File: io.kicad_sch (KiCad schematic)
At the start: 14 parts, among them SW6 TS-1088-AR02016, SW7 TS-1088-AR02016, SW8 TS-1088-AR02016, SW9 TS-1088-AR02016

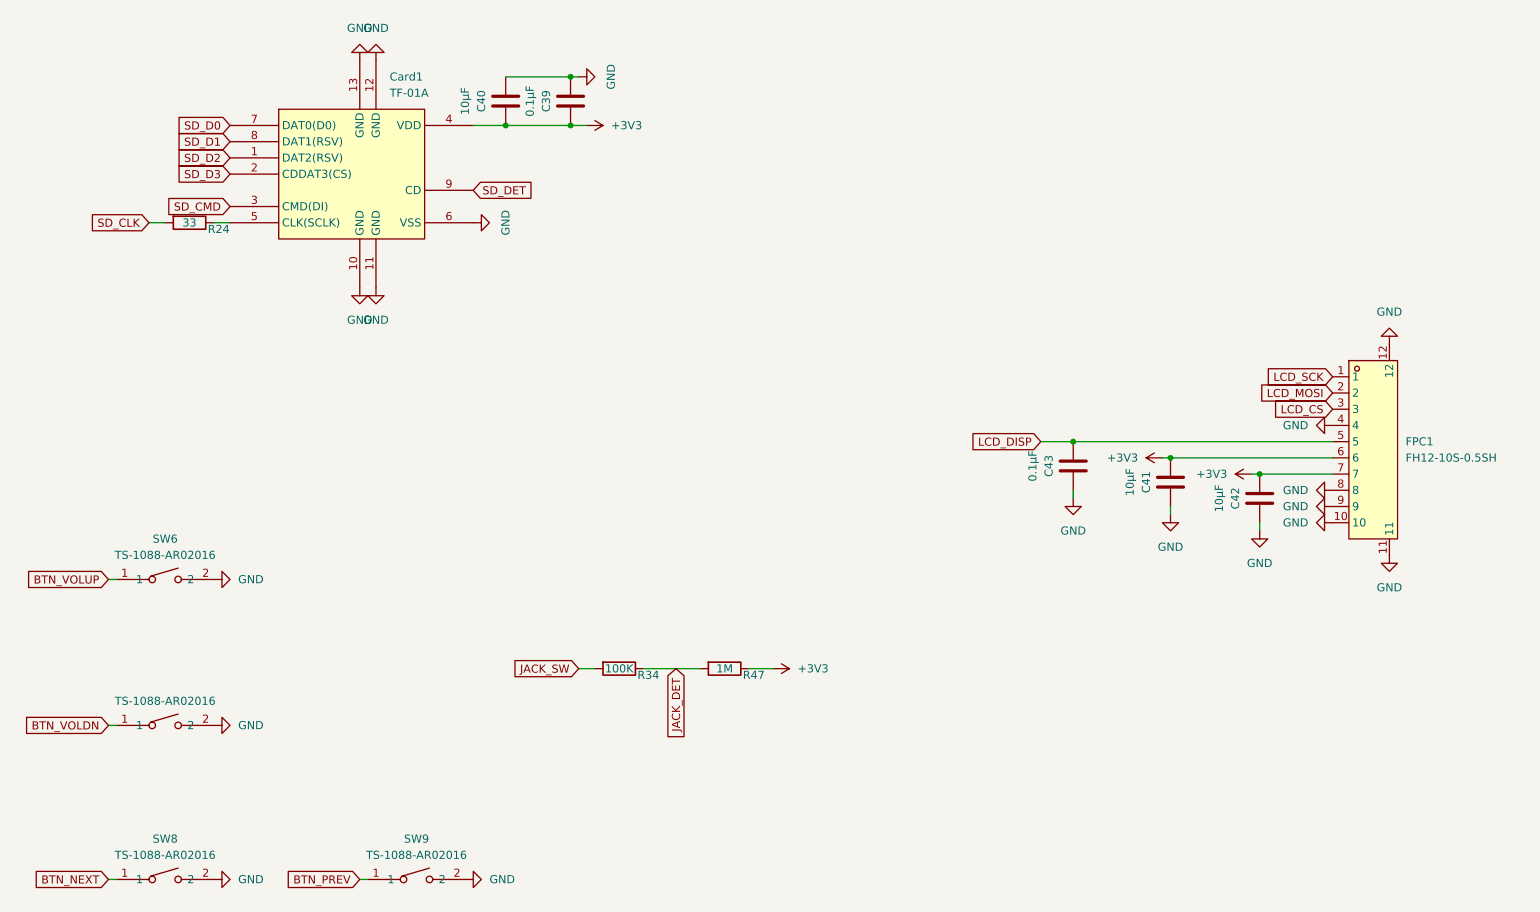
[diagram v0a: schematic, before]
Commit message: Schematic done
- sheet files renamed to English (usb, power, esp32, audio, io)
- final layout, annotation R1-R42 / C1-C43 / U1-U9 / J1-J4 / SW1-SW8
- all buttons are TS-1088, project R/C symbols, PWR_FLAGs
- connections.md replaces conexiuni.md (English, final references)
- final check on the KiCad netlist: 278/278 checks against connections.md
- status updated; firmware note: BQ25180 charge current defaults to ~10 mA

Co-Authored-By: Claude Opus 5.5 <noreply@anthropic.com>
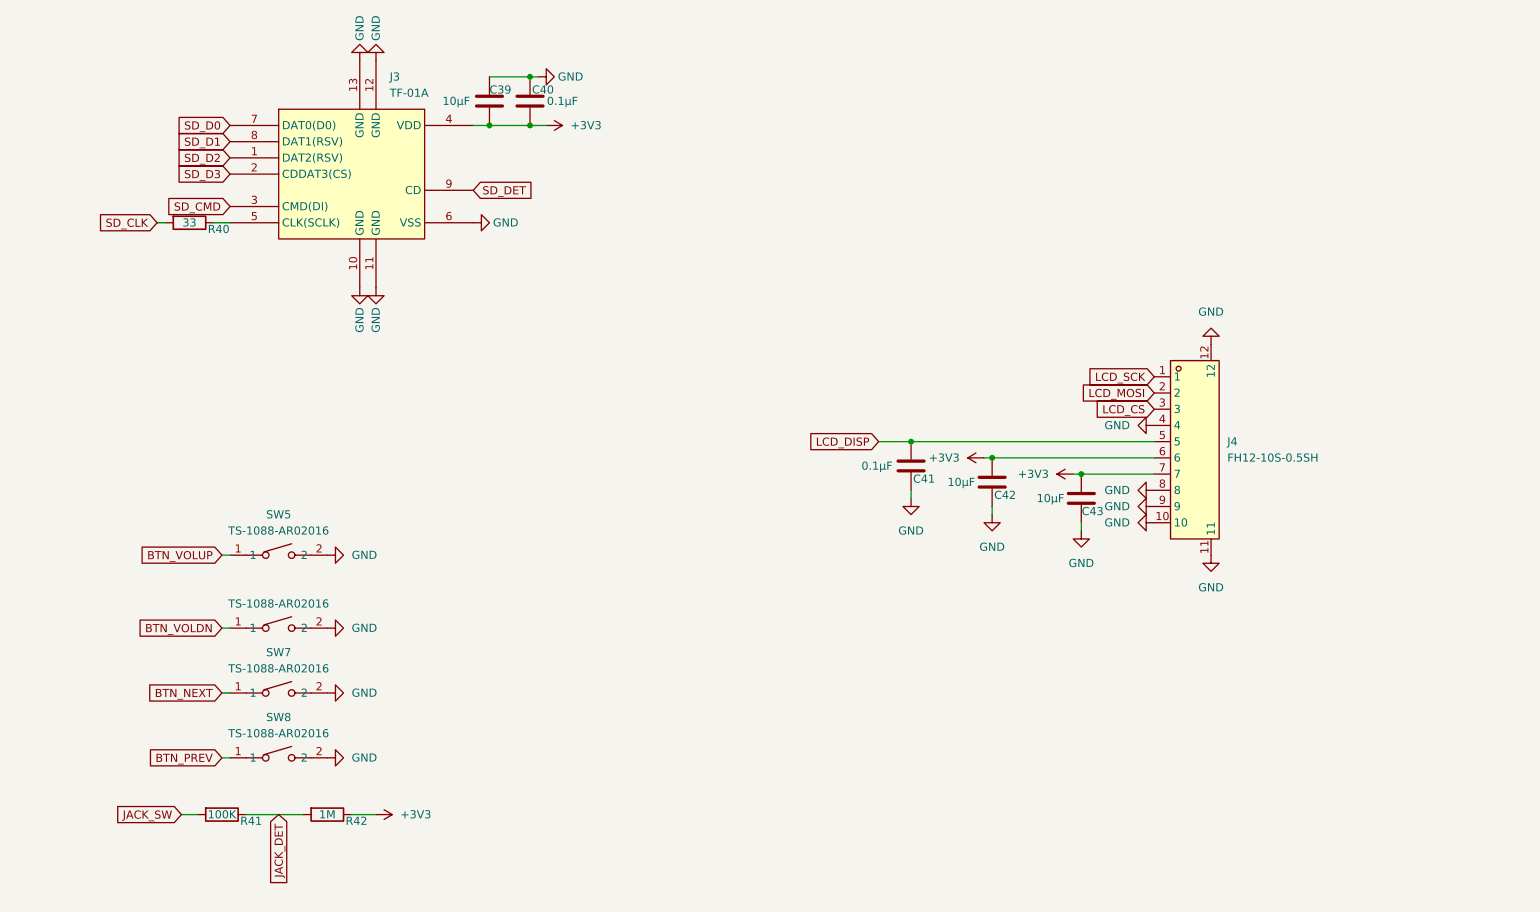
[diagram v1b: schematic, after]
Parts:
- R40: renamed from R24; symbol Device:R -> mp3_player:R
- R41: renamed from R34; symbol Device:R -> mp3_player:R
- R42: renamed from R47; symbol Device:R -> mp3_player:R
- renumbered C40 to C39, C39 to C40, C43 to C41, C41 to C42, C42 to C43, Card1 to J3, FPC1 to J4, SW6 to SW5, SW7 to SW6, SW8 to SW7, SW9 to SW8
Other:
- moved on the sheet: C39, C40, C41, C42, C43, J4, R41, R42, SW5, SW7, SW8

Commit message: Assign footprints and LCSC parts to passives, D2 and BT1
Thin-film 0.1% resistors in the audio path and rail dividers, C0G caps
in the DAC output filter, Samsung/Murata MLCCs with 0603/0805 cases for
bulk caps. Passive choices documented in mp3_player.md.

Co-Authored-By: Claude Opus 5.5 <noreply@anthropic.com>
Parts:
- C39, C42, C43: footprint (none) -> Capacitor_SMD:C_0603_1608Metric; LCSC Part (none) -> C19702
- C40, C41: footprint (none) -> Capacitor_SMD:C_0402_1005Metric; LCSC Part (none) -> C1525
- R40: footprint (none) -> Resistor_SMD:R_0402_1005Metric; LCSC Part (none) -> C25105
- R41: footprint (none) -> Resistor_SMD:R_0402_1005Metric; LCSC Part (none) -> C852472
- R42: footprint (none) -> Resistor_SMD:R_0402_1005Metric; LCSC Part (none) -> C26083
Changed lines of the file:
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@@
 			)
 		)
-		(property "Footprint" ""
+		(property "Footprint" "Capacitor_SMD:C_0603_1608Metric"
+			(at 191.4652 109.22 0)
+			(hide yes)
+			(show_name no)
+			(do_not_autoplace no)
+			(effects
+				(font
+					(size 1.27 1.27)
+				)
+			)
+		)
+				(property "LCSC Part" "C19702"
 			(at 191.4652 109.22 0)
 			(hide yes)
@@
 			)
 		)
-		(property "Footprint" ""
+		(property "Footprint" "Resistor_SMD:R_0402_1005Metric"
+			(at 86.36 155.702 90)
+			(hide yes)
+			(show_name no)
+			(do_not_autoplace no)
+			(effects
+				(font
+					(size 1.27 1.27)
+				)
+			)
+		)
+				(property "LCSC Part" "C26083"
 			(at 86.36 155.702 90)
 			(hide yes)
@@
 			)
 		)
-		(property "Footprint" ""
+		(property "Footprint" "Capacitor_SMD:C_0402_1005Metric"
+			(at 178.7652 106.68 0)
+			(hide yes)
+			(show_name no)
+			(do_not_autoplace no)
+			(effects
+				(font
+					(size 1.27 1.27)
+				)
+			)
+		)
+				(property "LCSC Part" "C1525"
 			(at 178.7652 106.68 0)
 			(hide yes)
@@
 			)
 		)
-		(property "Footprint" ""
+		(property "Footprint" "Capacitor_SMD:C_0402_1005Metric"
+			(at 119.0752 49.53 0)
+			(hide yes)
+			(show_name no)
+			(do_not_autoplace no)
+			(effects
+				(font
+					(size 1.27 1.27)
+				)
+			)
+		)
+				(property "LCSC Part" "C1525"
 			(at 119.0752 49.53 0)
 			(hide yes)
@@
 			)
 		)
-		(property "Footprint" ""
+		(property "Footprint" "Resistor_SMD:R_0402_1005Metric"
+			(at 69.85 155.702 90)
+			(hide yes)
+			(show_name no)
+			(do_not_autoplace no)
+			(effects
+				(font
+					(size 1.27 1.27)
+				)
+			)
+		)
+				(property "LCSC Part" "C852472"
 			(at 69.85 155.702 90)
 			(hide yes)
@@
 			)
 		)
-		(property "Footprint" ""
+		(property "Footprint" "Capacitor_SMD:C_0603_1608Metric"
+			(at 112.7252 49.53 0)
+			(hide yes)
+			(show_name no)
+			(do_not_autoplace no)
+			(effects
+				(font
+					(size 1.27 1.27)
+				)
+			)
+		)
+				(property "LCSC Part" "C19702"
 			(at 112.7252 49.53 0)
 			(hide yes)
@@
 			)
 		)
-		(property "Footprint" ""
+		(property "Footprint" "Resistor_SMD:R_0402_1005Metric"
+			(at 64.77 62.992 90)
+			(hide yes)
+			(show_name no)
+			(do_not_autoplace no)
+			(effects
+				(font
+					(size 1.27 1.27)
+				)
+			)
+		)
+				(property "LCSC Part" "C25105"
 			(at 64.77 62.992 90)
 			(hide yes)
@@
 			)
 		)
-		(property "Footprint" ""
+		(property "Footprint" "Capacitor_SMD:C_0603_1608Metric"
 			(at 205.4352 111.76 0)
 			(hide yes)
+			(show_name no)
+			(do_not_autoplace no)
+			(effects
+				(font
+					(size 1.27 1.27)
+				)
+			)
+		)
+				(property "LCSC Part" "C19702"
+			(at 205.4352 111.76 0)
+			(hide yes)

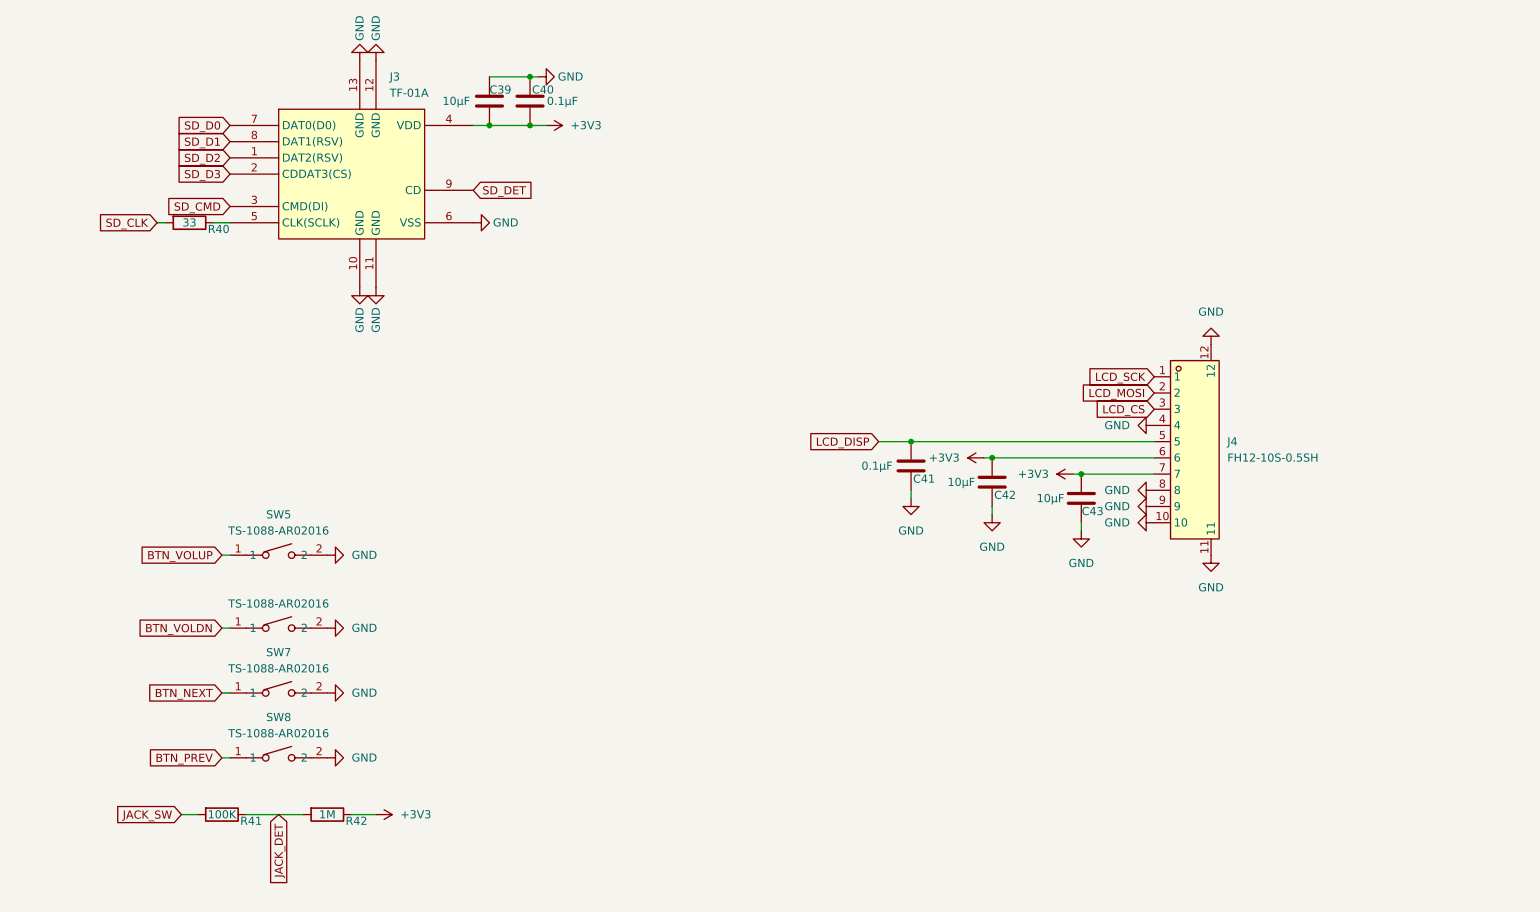
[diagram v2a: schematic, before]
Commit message: Fix ERC and document enclosure concept
- ERC clean: power flags moved onto real nets, USBLC6 pin types,
  Unspecified pins allowed in the pin conflict map, off-grid wires aligned
- mp3_player.md: enclosure section (anodized aluminium v1, titanium v2,
  printed click wheel and antenna cap, build123d workflow)
- ignore the build123d venv

Co-Authored-By: Claude Opus 5.5 <noreply@anthropic.com>
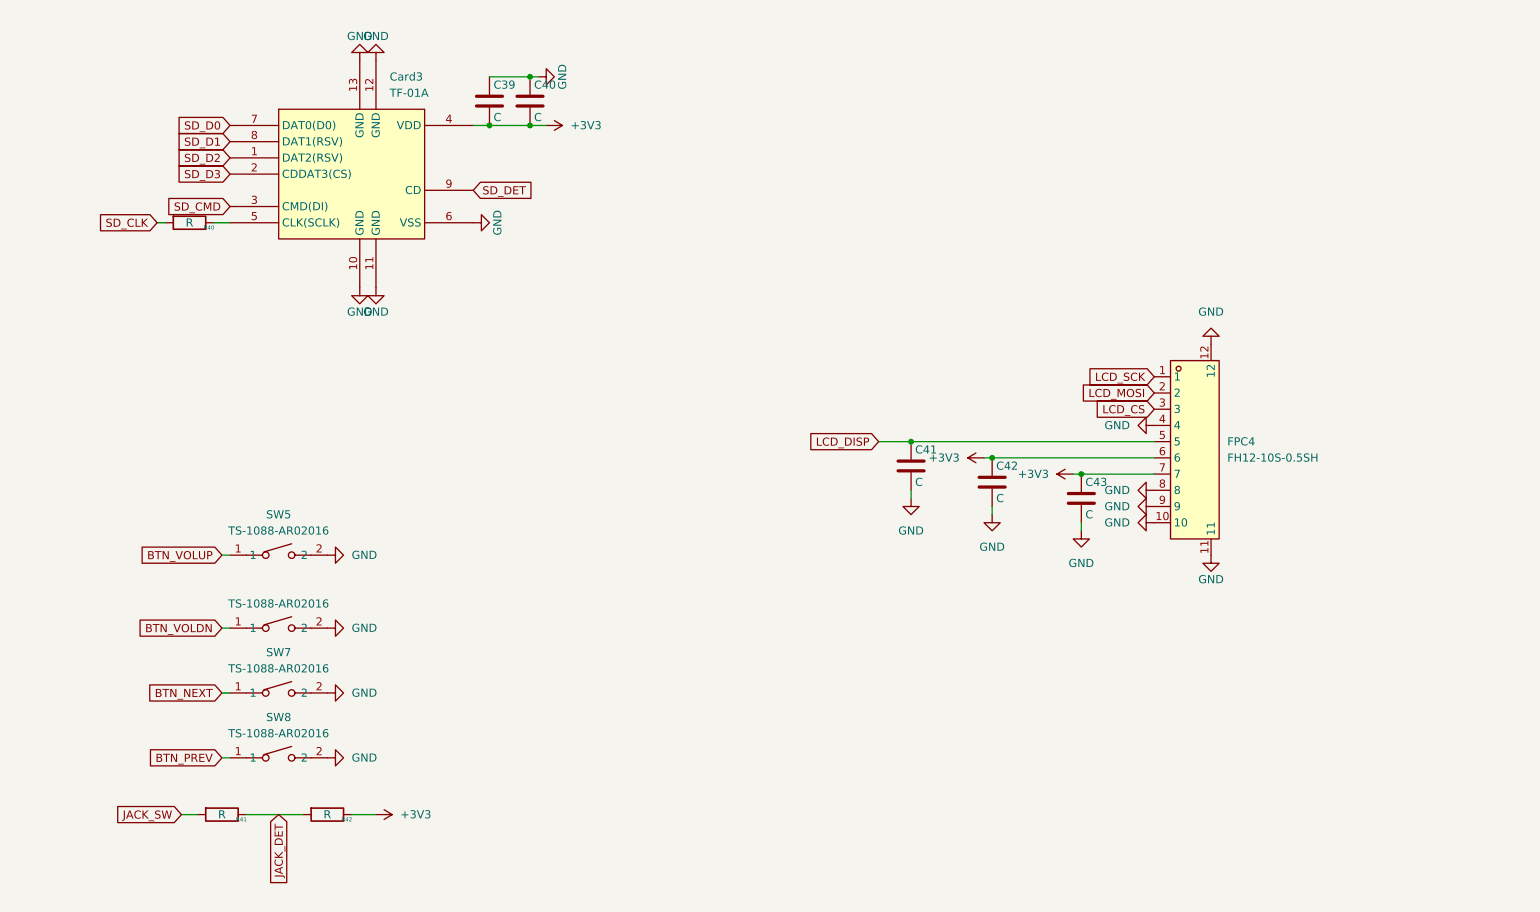
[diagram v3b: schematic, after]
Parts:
- C39, C42, C43: value 10µF -> C
- C40, C41: value 0.1µF -> C
- R40: value 33 -> R
- R41: value 100K -> R
- R42: value 1M -> R
- renumbered J3 to Card3, J4 to FPC4

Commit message: Schematic and parts for enclosure B
- jack PJ-342C CB (TRRS, sinking) as CN1, HP-DET on JACK_SW, MIC to GND,
  100nF on JACK_DET (detect is now active low)
- USB-C TYPE-C 16P CB0.8 073 (sinking, 0.8 mm board) as USB1
- BT1 on JST SH SM02B-SRSS-TB, click wheel on TS-1187B-B (0.75 mm),
  power on EVQP7J01P side switch
- new footprints/3D models in lib; switch and JST SH footprints renumbered
  so the existing 2-pin symbols fit
- enclosure: power key on the right side, level with the display
- docs: connections.md, code.md and BOM updated

ERC: 0 errors, 0 warnings.

Co-Authored-By: Claude Opus 5.5 <noreply@anthropic.com>
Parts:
- SW5, SW6, SW7, SW8: value TS-1088-AR02016 -> TS-1187B-B; footprint mp3_player:SW-SMD_L3.9-W3.0-P4.45 -> mp3_player:KEY-SMD_4P-L4.8-W4.8-P3.70-LS6.4-TL; LCSC Part C720477 -> C500066
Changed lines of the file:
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@@
 			)
 		)
-		(property "Value" "TS-1088-AR02016"
+		(property "Value" "TS-1187B-B"
 			(at 78.74 113.03 0)
 			(show_name no)
@@
 			)
 		)
-		(property "Footprint" "mp3_player:SW-SMD_L3.9-W3.0-P4.45"
+		(property "Footprint" "mp3_player:KEY-SMD_4P-L4.8-W4.8-P3.70-LS6.4-TL"
 			(at 78.74 124.46 0)
 			(hide yes)
@@
 			)
 		)
-		(property "LCSC Part" "C720477"
+		(property "LCSC Part" "C500066"
 			(at 78.74 134.62 0)
 			(hide yes)
@@
 			)
 		)
-		(property "Value" "TS-1088-AR02016"
+		(property "Value" "TS-1187B-B"
 			(at 78.74 144.78 0)
 			(show_name no)
@@
 			)
 		)
-		(property "Footprint" "mp3_player:SW-SMD_L3.9-W3.0-P4.45"
+		(property "Footprint" "mp3_player:KEY-SMD_4P-L4.8-W4.8-P3.70-LS6.4-TL"
 			(at 78.74 156.21 0)
 			(hide yes)
@@
 			)
 		)
-		(property "LCSC Part" "C720477"
+		(property "LCSC Part" "C500066"
 			(at 78.74 166.37 0)
 			(hide yes)
@@
 			)
 		)
-		(property "Value" "TS-1088-AR02016"
+		(property "Value" "TS-1187B-B"
 			(at 78.74 124.46 0)
 			(show_name no)
@@
 			)
 		)
-		(property "Footprint" "mp3_player:SW-SMD_L3.9-W3.0-P4.45"
+		(property "Footprint" "mp3_player:KEY-SMD_4P-L4.8-W4.8-P3.70-LS6.4-TL"
 			(at 78.74 135.89 0)
 			(hide yes)
@@
 			)
 		)
-		(property "LCSC Part" "C720477"
+		(property "LCSC Part" "C500066"
 			(at 78.74 146.05 0)
 			(hide yes)
@@
 			)
 		)
-		(property "Value" "TS-1088-AR02016"
+		(property "Value" "TS-1187B-B"
 			(at 78.74 134.62 0)
 			(show_name no)
@@
 			)
 		)
-		(property "Footprint" "mp3_player:SW-SMD_L3.9-W3.0-P4.45"
+		(property "Footprint" "mp3_player:KEY-SMD_4P-L4.8-W4.8-P3.70-LS6.4-TL"
 			(at 78.74 146.05 0)
 			(hide yes)
@@
 			)
 		)
-		(property "LCSC Part" "C720477"
+		(property "LCSC Part" "C500066"
 			(at 78.74 156.21 0)
 			(hide yes)

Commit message: Display connector: FH19C-10S, placed under the display
- FH12 (2.0 mm) fits neither side of the board; FH19C-10S-0.5SH(10)
  (C598004) is 0.9 mm tall, bottom contact, same 10 pins
- footprint and 3D model from LCSC added to the project library;
  schematic fields (value, footprint, datasheet, LCSC) updated
- FPC4 on the front at (149.1, 110.1), opening toward the display: the
  LCD tail lies flat into it, flex pin 1 and connector pin 1 both on
  the right
- docs: BOM, placement checklist and connections.md follow the swap

Co-Authored-By: Claude Opus 5.5 <noreply@anthropic.com>
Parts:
- FPC4: value FH12-10S-0.5SH -> FH19C-10S-0.5SH(10); footprint mp3_player:FPC-SMD_FH12-10S-0.5SH-55 -> mp3_player:FPC-SMD_10P-P0.50_FH19C-10S-0.5SH-10; LCSC Part C506791 -> C598004
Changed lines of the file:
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@@
 			)
 		)
-		(property "Value" "FH12-10S-0.5SH"
+		(property "Value" "FH19C-10S-0.5SH(10)"
 			(at 227.33 101.5999 0)
 			(show_name no)
@@
 			)
 		)
-		(property "Footprint" "mp3_player:FPC-SMD_FH12-10S-0.5SH-55"
+		(property "Footprint" "mp3_player:FPC-SMD_10P-P0.50_FH19C-10S-0.5SH-10"
 			(at 220.98 124.46 0)
 			(hide yes)
@@
 			)
 		)
-		(property "Datasheet" "https://lcsc.com/product-detail/FFC-FPC-Connectors_HRS-Hirose-HRS-FH12-10S-0-5SH-55_C506791.html"
+		(property "Datasheet" "https://www.lcsc.com/datasheet/lcsc_datasheet_2410010404_HRS-Hirose-FH19C-10S-0-5SH-10_C598004.pdf"
 			(at 220.98 127 0)
 			(hide yes)
@@
 			)
 		)
-		(property "LCSC Part" "C506791"
+		(property "LCSC Part" "C598004"
 			(at 220.98 134.62 0)
 			(hide yes)
